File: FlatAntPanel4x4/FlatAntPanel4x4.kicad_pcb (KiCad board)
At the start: 4 copper layers, 186 x 226 mm, 124 parts

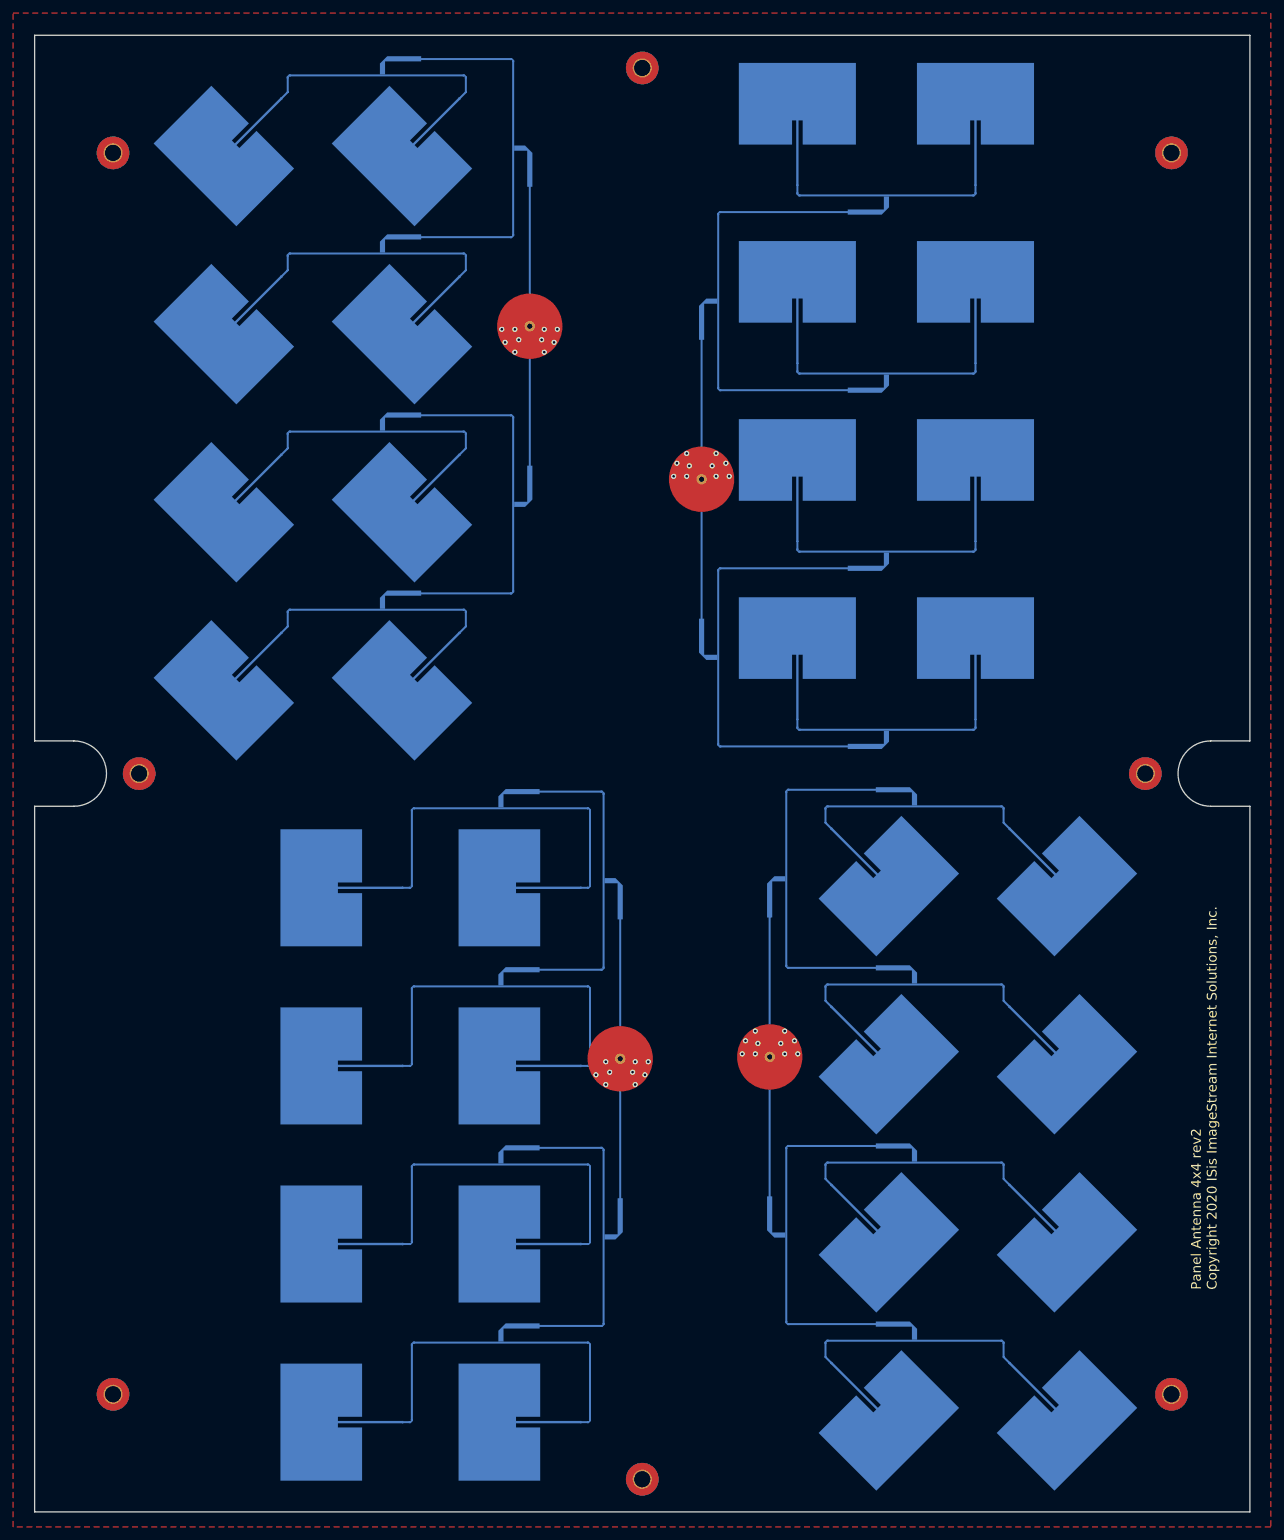
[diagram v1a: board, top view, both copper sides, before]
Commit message: Restore old 4x4 flat antenna. Modify 4 polarity to be 2 pol.
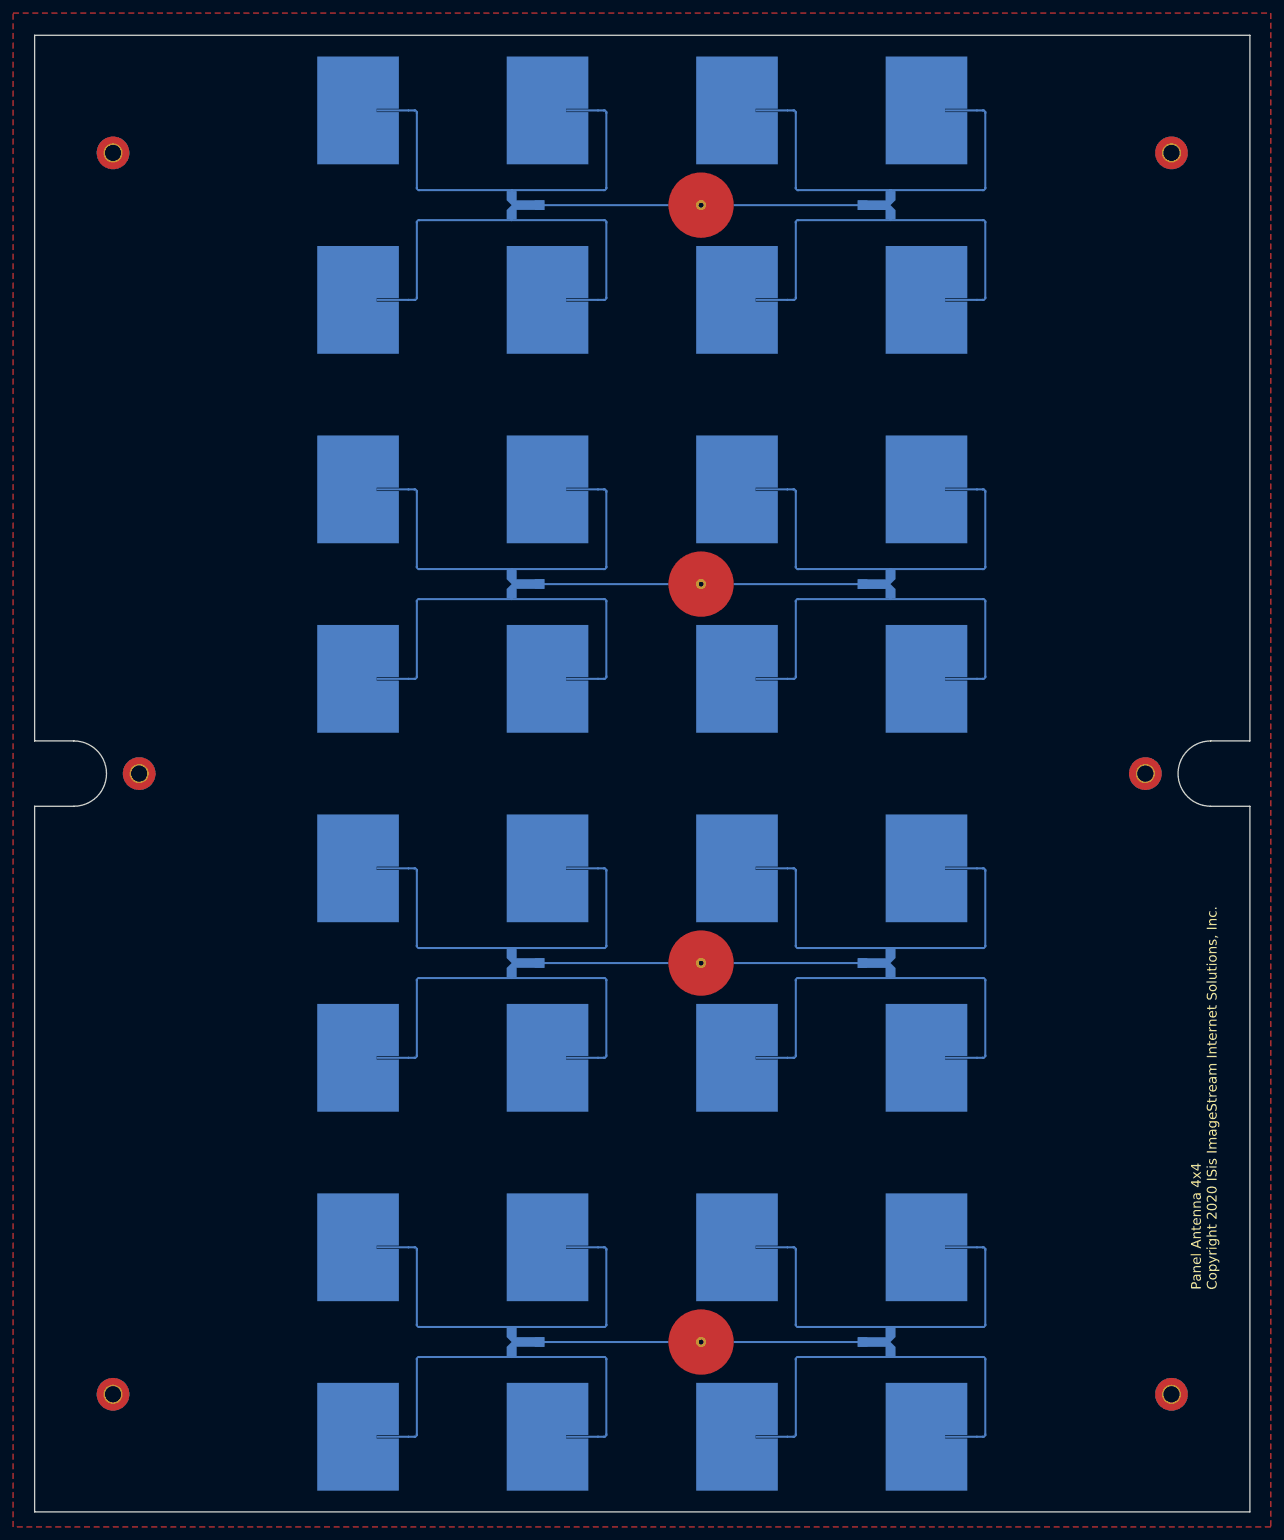
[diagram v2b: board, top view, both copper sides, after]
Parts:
- removed the AA10 at (144.0, 24.5)
- removed the AA10 at (57.7, 118.3)
- removed the AA10 at (144.0, 106.3)
- removed the AA10 at (144.0, 51.8)
- removed the AA10 at (57.7, 172.8)
- removed the AA10 at (57.7, 145.6)
- removed the AA10 at (57.7, 200.1)
- removed the AA10 at (144.0, 79.0)
- removed the AA11 at (85.0, 172.8)
- removed the AA11 at (116.7, 79.0)
- removed the AA11 at (85.0, 200.1)
- removed the AA11 at (116.7, 24.5)
- removed the AA11 at (116.7, 106.3)
- removed the AA11 at (85.0, 118.3)
- removed the AA11 at (116.7, 51.8)
- removed the AA11 at (85.0, 145.6)
- removed the AA12 at (85.0, 185.0)
- removed the AA12 at (85.0, 157.7)
- removed the AA12 at (85.0, 212.3)
- removed the AA12 at (85.0, 130.5)
- removed the AA15 at (104.6, 108.8)
- removed the AA15 at (104.6, 81.6)
- removed the AA15 at (104.6, 54.3)
- removed the AA15 at (87.1, 197.5)
- removed the AA15 at (87.1, 143.0)
- removed the AA15 at (104.6, 27.1)
- removed the AA15 at (87.1, 115.8)
- removed the AA15 at (87.1, 170.3)
- removed the AA5 at (121.0, 199.8)
- removed the AA5 at (148.3, 118.0)
- removed the AA5 at (73.2, 85.4)
- removed the AA5 at (121.0, 145.3)
- removed the AA5 at (148.3, 172.5)
- removed the AA5 at (121.0, 172.5)
- removed the AA5 at (73.2, 30.9)
- removed the AA5 at (73.2, 58.2)
- removed the AA5 at (115.0, 115.5)
- removed the AA5 at (73.2, 3.64)
- removed the AA5 at (38.7, 60.7)
- removed the AA5 at (121.0, 118.0)
- removed the AA5 at (38.7, 87.9)
- removed the AA5 at (115.0, 197.3)
- removed the AA5 at (38.7, 6.14)
- removed the AA5 at (115.0, 142.7)
- removed the AA5 at (66.0, 33.4)
- removed the AA5 at (66.0, 87.9)
- removed the AA5 at (148.3, 145.3)
- removed the AA5 at (38.7, 33.4)
- removed the AA5 at (66.0, 6.14)
- removed the AA5 at (115.0, 170.0)
- removed the AA5 at (148.3, 199.8)
- removed the AA5 at (66.0, 60.7)
- removed the AA9 at (57.7, 212.3)
- removed the AA9 at (57.7, 157.7)
- removed the AA9 at (57.7, 185.0)
- removed the AA9 at (57.7, 130.5)
- removed the AE1 at (43.9, 157.7)
- removed the AE1 at (56.2, 100.3)
- removed the AE1 at (158.0, 157.5)
- removed the AE2 at (29.0, 18.5)
- removed the AE2 at (71.1, 157.7)
- removed the AE2 at (158.0, 130.2)
- removed the AE3 at (29.0, 73.0)
- removed the AE3 at (43.9, 130.5)
- removed the AE3 at (130.7, 157.5)
- removed the AE4 at (71.1, 130.5)
- removed the AE4 at (130.7, 130.2)
- removed the AE4 at (29.0, 45.7)
- removed the AE5 at (43.9, 212.3)
- removed the AE5 at (158.0, 212.0)
- removed the AE5 at (56.2, 45.7)
- removed the AE6 at (56.2, 73.0)
- removed the AE6 at (71.1, 212.3)
- removed the AE6 at (158.0, 184.7)
- removed the AE7 at (56.2, 18.5)
- removed the AE7 at (130.7, 212.0)
- removed the AE7 at (43.9, 185.0)
- removed the AE8 at (130.7, 184.7)
- removed the AE8 at (71.1, 185.0)
- removed the AE8 at (29.0, 100.3)
- removed Feed1 (x4): Feed1, Scott:Flat_Ant_Hole
- removed H10, H9: Mounting Hole, MountingHole:MountingHole_2.5mm_Pad_TopBottom
- removed REF** (x16): RF-Transformer-70.71ohm, Scott-RF-JLCPCB-1.2mm7628-4layer:RF-Transformer-70.71ohm
- removed REF** (x8): RF-Transformer-70.71ohm-Right, Scott-RF-JLCPCB-1.2mm7628-4layer:RF-Transformer-70.71ohm-Right
- added AA1: RFAngle, Scott:RF-Angle-100ohm, B.Cu at (116.5, 98.5)
- added AA1: RFAngle, Scott:RF-Angle-100ohm, B.Cu at (116.5, 40.5)
- added AA1: RFAngle, Scott:RF-Angle-100ohm, B.Cu at (116.5, 156.5)
- added AA1: RFAngle, Scott:RF-Angle-100ohm, B.Cu at (116.5, 214.5)
- added AA10: RFAngle, Scott:RF-Angle-100ohm, B.Cu at (58.5, 86.3)
- added AA10: RFAngle, Scott:RF-Angle-100ohm, B.Cu at (58.5, 202.3)
- added AA10: RFAngle, Scott:RF-Angle-100ohm, B.Cu at (58.5, 144.3)
- added AA10: RFAngle, Scott:RF-Angle-100ohm, B.Cu at (58.5, 28.3)
- added AA11: RFAngle, Scott:RF-Angle-100ohm, B.Cu at (87.5, 144.3)
- added AA11: RFAngle, Scott:RF-Angle-100ohm, B.Cu at (87.5, 202.3)
- added AA11: RFAngle, Scott:RF-Angle-100ohm, B.Cu at (87.5, 28.3)
- added AA11: RFAngle, Scott:RF-Angle-100ohm, B.Cu at (87.5, 86.3)
- added AA12: RFAngle, Scott:RF-Angle-100ohm, B.Cu at (87.5, 156.5)
- added AA12: RFAngle, Scott:RF-Angle-100ohm, B.Cu at (87.5, 98.5)
- added AA12: RFAngle, Scott:RF-Angle-100ohm, B.Cu at (87.5, 214.5)
- added AA12: RFAngle, Scott:RF-Angle-100ohm, B.Cu at (87.5, 40.5)
- added AA13: RFAngle, Scott:RF-Angle-100ohm, B.Cu at (58.5, 127.5)
- added AA13: RFAngle, Scott:RF-Angle-100ohm, B.Cu at (58.5, 185.5)
- added AA13: RFAngle, Scott:RF-Angle-100ohm, B.Cu at (58.5, 69.5)
- added AA13: RFAngle, Scott:RF-Angle-100ohm, B.Cu at (58.5, 11.5)
- added AA14: RFAngle, Scott:RF-Angle-100ohm, B.Cu at (58.5, 139.7)
- added AA14: RFAngle, Scott:RF-Angle-100ohm, B.Cu at (58.5, 197.7)
- added AA14: RFAngle, Scott:RF-Angle-100ohm, B.Cu at (58.5, 81.7)
- added AA14: RFAngle, Scott:RF-Angle-100ohm, B.Cu at (58.5, 23.7)
- added AA15: RFAngle, Scott:RF-Angle-100ohm, B.Cu at (87.5, 81.7)
- added AA15: RFAngle, Scott:RF-Angle-100ohm, B.Cu at (87.5, 197.7)
- added AA15: RFAngle, Scott:RF-Angle-100ohm, B.Cu at (87.5, 139.7)
- added AA15: RFAngle, Scott:RF-Angle-100ohm, B.Cu at (87.5, 23.7)
- added AA16: RFAngle, Scott:RF-Angle-100ohm, B.Cu at (87.5, 69.5)
- added AA16: RFAngle, Scott:RF-Angle-100ohm, B.Cu at (87.5, 11.5)
- added AA16: RFAngle, Scott:RF-Angle-100ohm, B.Cu at (87.5, 127.5)
- added AA16: RFAngle, Scott:RF-Angle-100ohm, B.Cu at (87.5, 185.5)
- added AA2: RFAngle, Scott:RF-Angle-100ohm, B.Cu at (116.5, 28.3)
- added AA2: RFAngle, Scott:RF-Angle-100ohm, B.Cu at (116.5, 202.3)
- added AA2: RFAngle, Scott:RF-Angle-100ohm, B.Cu at (116.5, 144.3)
- added AA2: RFAngle, Scott:RF-Angle-100ohm, B.Cu at (116.5, 86.3)
- added AA3: RFAngle, Scott:RF-Angle-100ohm, B.Cu at (145.5, 144.3)
- added AA3: RFAngle, Scott:RF-Angle-100ohm, B.Cu at (145.5, 202.3)
- added AA3: RFAngle, Scott:RF-Angle-100ohm, B.Cu at (145.5, 86.3)
- added AA3: RFAngle, Scott:RF-Angle-100ohm, B.Cu at (145.5, 28.3)
- added AA4: RFAngle, Scott:RF-Angle-100ohm, B.Cu at (145.5, 40.5)
- added AA4: RFAngle, Scott:RF-Angle-100ohm, B.Cu at (145.5, 214.5)
- added AA4: RFAngle, Scott:RF-Angle-100ohm, B.Cu at (145.5, 98.5)
- added AA4: RFAngle, Scott:RF-Angle-100ohm, B.Cu at (145.5, 156.5)
- added AA5: RFAngle, Scott:RF-Angle-100ohm, B.Cu at (116.5, 185.5)
- added AA5: RFAngle, Scott:RF-Angle-100ohm, B.Cu at (116.5, 127.5)
- added AA5: RFAngle, Scott:RF-Angle-100ohm, B.Cu at (116.5, 69.5)
- added AA5: RFAngle, Scott:RF-Angle-100ohm, B.Cu at (116.5, 11.5)
- added AA6: RFAngle, Scott:RF-Angle-100ohm, B.Cu at (116.5, 23.7)
- added AA6: RFAngle, Scott:RF-Angle-100ohm, B.Cu at (116.5, 197.7)
- added AA6: RFAngle, Scott:RF-Angle-100ohm, B.Cu at (116.5, 139.7)
- added AA6: RFAngle, Scott:RF-Angle-100ohm, B.Cu at (116.5, 81.7)
- added AA7: RFAngle, Scott:RF-Angle-100ohm, B.Cu at (145.5, 81.7)
- added AA7: RFAngle, Scott:RF-Angle-100ohm, B.Cu at (145.5, 197.7)
- added AA7: RFAngle, Scott:RF-Angle-100ohm, B.Cu at (145.5, 23.7)
- added AA7: RFAngle, Scott:RF-Angle-100ohm, B.Cu at (145.5, 139.7)
- added AA8: RFAngle, Scott:RF-Angle-100ohm, B.Cu at (145.5, 127.5)
- added AA8: RFAngle, Scott:RF-Angle-100ohm, B.Cu at (145.5, 11.5)
- added AA8: RFAngle, Scott:RF-Angle-100ohm, B.Cu at (145.5, 69.5)
- added AA8: RFAngle, Scott:RF-Angle-100ohm, B.Cu at (145.5, 185.5)
- added AA9: RFAngle, Scott:RF-Angle-100ohm, B.Cu at (58.5, 156.5)
- added AA9: RFAngle, Scott:RF-Angle-100ohm, B.Cu at (58.5, 40.5)
- added AA9: RFAngle, Scott:RF-Angle-100ohm, B.Cu at (58.5, 214.5)
- added AA9: RFAngle, Scott:RF-Angle-100ohm, B.Cu at (58.5, 98.5)
- added AE1: Antenna, Scott:PanelAnt5.0_V_UP_100R, B.Cu at (107.5, 40.5)
- added AE1: Antenna, Scott:PanelAnt5.0_V_UP_100R, B.Cu at (107.5, 156.5)
- added AE1: Antenna, Scott:PanelAnt5.0_V_UP_100R, B.Cu at (107.5, 98.5)
- added AE2: Antenna, Scott:PanelAnt5.0_V_UP_100R, B.Cu at (136.5, 156.5)
- added AE2: Antenna, Scott:PanelAnt5.0_V_UP_100R, B.Cu at (136.5, 40.5)
- added AE2: Antenna, Scott:PanelAnt5.0_V_UP_100R, B.Cu at (136.5, 98.5)
- added AE3: Antenna, Scott:PanelAnt5.0_V_UP_100R, B.Cu at (107.5, 11.5)
- added AE3: Antenna, Scott:PanelAnt5.0_V_UP_100R, B.Cu at (107.5, 69.5)
- added AE3: Antenna, Scott:PanelAnt5.0_V_UP_100R, B.Cu at (107.5, 127.5)
- added AE4: Antenna, Scott:PanelAnt5.0_V_UP_100R, B.Cu at (136.5, 127.5)
- added AE4: Antenna, Scott:PanelAnt5.0_V_UP_100R, B.Cu at (136.5, 11.5)
- added AE4: Antenna, Scott:PanelAnt5.0_V_UP_100R, B.Cu at (136.5, 69.5)
- added AE5: Antenna, Scott:PanelAnt5.0_V_UP_100R, B.Cu at (49.5, 98.5)
- added AE5: Antenna, Scott:PanelAnt5.0_V_UP_100R, B.Cu at (49.5, 40.5)
- added AE5: Antenna, Scott:PanelAnt5.0_V_UP_100R, B.Cu at (49.5, 156.5)
- added AE6: Antenna, Scott:PanelAnt5.0_V_UP_100R, B.Cu at (78.5, 98.5)
- added AE6: Antenna, Scott:PanelAnt5.0_V_UP_100R, B.Cu at (78.5, 40.5)
- added AE6: Antenna, Scott:PanelAnt5.0_V_UP_100R, B.Cu at (78.5, 156.5)
- added AE7: Antenna, Scott:PanelAnt5.0_V_UP_100R, B.Cu at (49.5, 127.5)
- added AE7: Antenna, Scott:PanelAnt5.0_V_UP_100R, B.Cu at (49.5, 69.5)
- added AE7: Antenna, Scott:PanelAnt5.0_V_UP_100R, B.Cu at (49.5, 11.5)
- added AE8: Antenna, Scott:PanelAnt5.0_V_UP_100R, B.Cu at (78.5, 127.5)
- added AE8: Antenna, Scott:PanelAnt5.0_V_UP_100R, B.Cu at (78.5, 11.5)
- added AE8: Antenna, Scott:PanelAnt5.0_V_UP_100R, B.Cu at (78.5, 69.5)
- added FEED 1: Feed1, Scott:Flat_Ant_Hole, B.Cu at (102.0, 26.0)
- added FEED 2: Feed1, Scott:Flat_Ant_Hole, B.Cu at (102.0, 84.0)
- added FEED 3: Feed1, Scott:Flat_Ant_Hole, B.Cu at (102.0, 142.0)
- added FEED 4: Feed1, Scott:Flat_Ant_Hole, B.Cu at (102.0, 200.0)
- added NT1: NetTie_3_Tee, Scott:RF-T-50ohm, B.Cu at (131.0, 84.0)
- added NT1: NetTie_3_Tee, Scott:RF-T-50ohm, B.Cu at (131.0, 142.0)
- added NT1: NetTie_3_Tee, Scott:RF-T-50ohm, B.Cu at (131.0, 26.0)
- added NT1: NetTie_3_Tee, Scott:RF-T-50ohm, B.Cu at (131.0, 200.0)
- added NT2: NetTie_3_Tee, Scott:RF-T-50ohm, B.Cu at (73.0, 200.0)
- added NT2: NetTie_3_Tee, Scott:RF-T-50ohm, B.Cu at (73.0, 26.0)
- added NT2: NetTie_3_Tee, Scott:RF-T-50ohm, B.Cu at (73.0, 142.0)
- added NT2: NetTie_3_Tee, Scott:RF-T-50ohm, B.Cu at (73.0, 84.0)
- AE1, AE2, AE3, AE4, AE5, AE6, AE7, AE8: footprint Scott-RF-JLCPCB-1.2mm7628-4layer:Patch_Inset_5.5_Linear_7.1dBi_100R -> Scott:PanelAnt5.0_V_UP_100R
- moved AE5 214.8 mm to (49.5, 214.5), turned to 90 degrees
- moved AE7 198.9 mm to (49.5, 185.5), turned to 90 degrees
- moved AE6 180.8 mm to (78.5, 214.5), turned to 90 degrees
- moved AE8 161.6 mm to (78.5, 185.5), turned to 90 degrees
- moved AE1 149.8 mm to (107.5, 214.5), turned to 90 degrees
- moved AE3 125.9 mm to (107.5, 185.5), turned to 90 degrees
- moved AE2 123.8 mm to (136.5, 214.5), turned to 90 degrees
- moved AE4 93.5 mm to (136.5, 185.5), turned to 90 degrees
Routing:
- net /A1E3S2: track 293.9 -> 46.4 mm
- net /A1P1: track 397.6 -> 196.0 mm
- net /A1E3: track 194.7 -> 3.81 mm
- net /A1P3: track 0.00 -> 116.9 mm
- net /A1P2: track 0.00 -> 116.9 mm
- net /A1P5: track 0.00 -> 116.4 mm
- net /A1P4: track 212.9 -> 117.1 mm
- net /A1E4S2: track 0.00 -> 46.4 mm
- net /A1E8S2: track 0.00 -> 46.3 mm
- net /A1E7S2: track 0.00 -> 46.3 mm
- net /A1E1S2: track 0.00 -> 45.6 mm
- net /A1E2S2: track 0.00 -> 45.6 mm
- net /A1E6S2: track 51.2 -> 45.6 mm
- net /A1E5S2: track 51.3 -> 46.0 mm
- net /A1E8: track 0.00 -> 3.88 mm
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- added copper zone on F.Cu, net GND
- removed copper zone on F.Cu, net (none)
- removed copper zone on In1.Cu, net GND
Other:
- copper layers 4 -> 2
- board text added: "Panel Antenna 4x4 Copyright 2020 ISis ImageStream Internet Solutions, Inc."
- board text removed: "Panel Antenna 4x4 rev2 Copyright 2020 ISis ImageStream Internet Solutions, Inc."

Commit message: Many enhancements to the AP3000 board. Reworking FlatAntPanel4x4 again with proper holes Made a connector test pcb
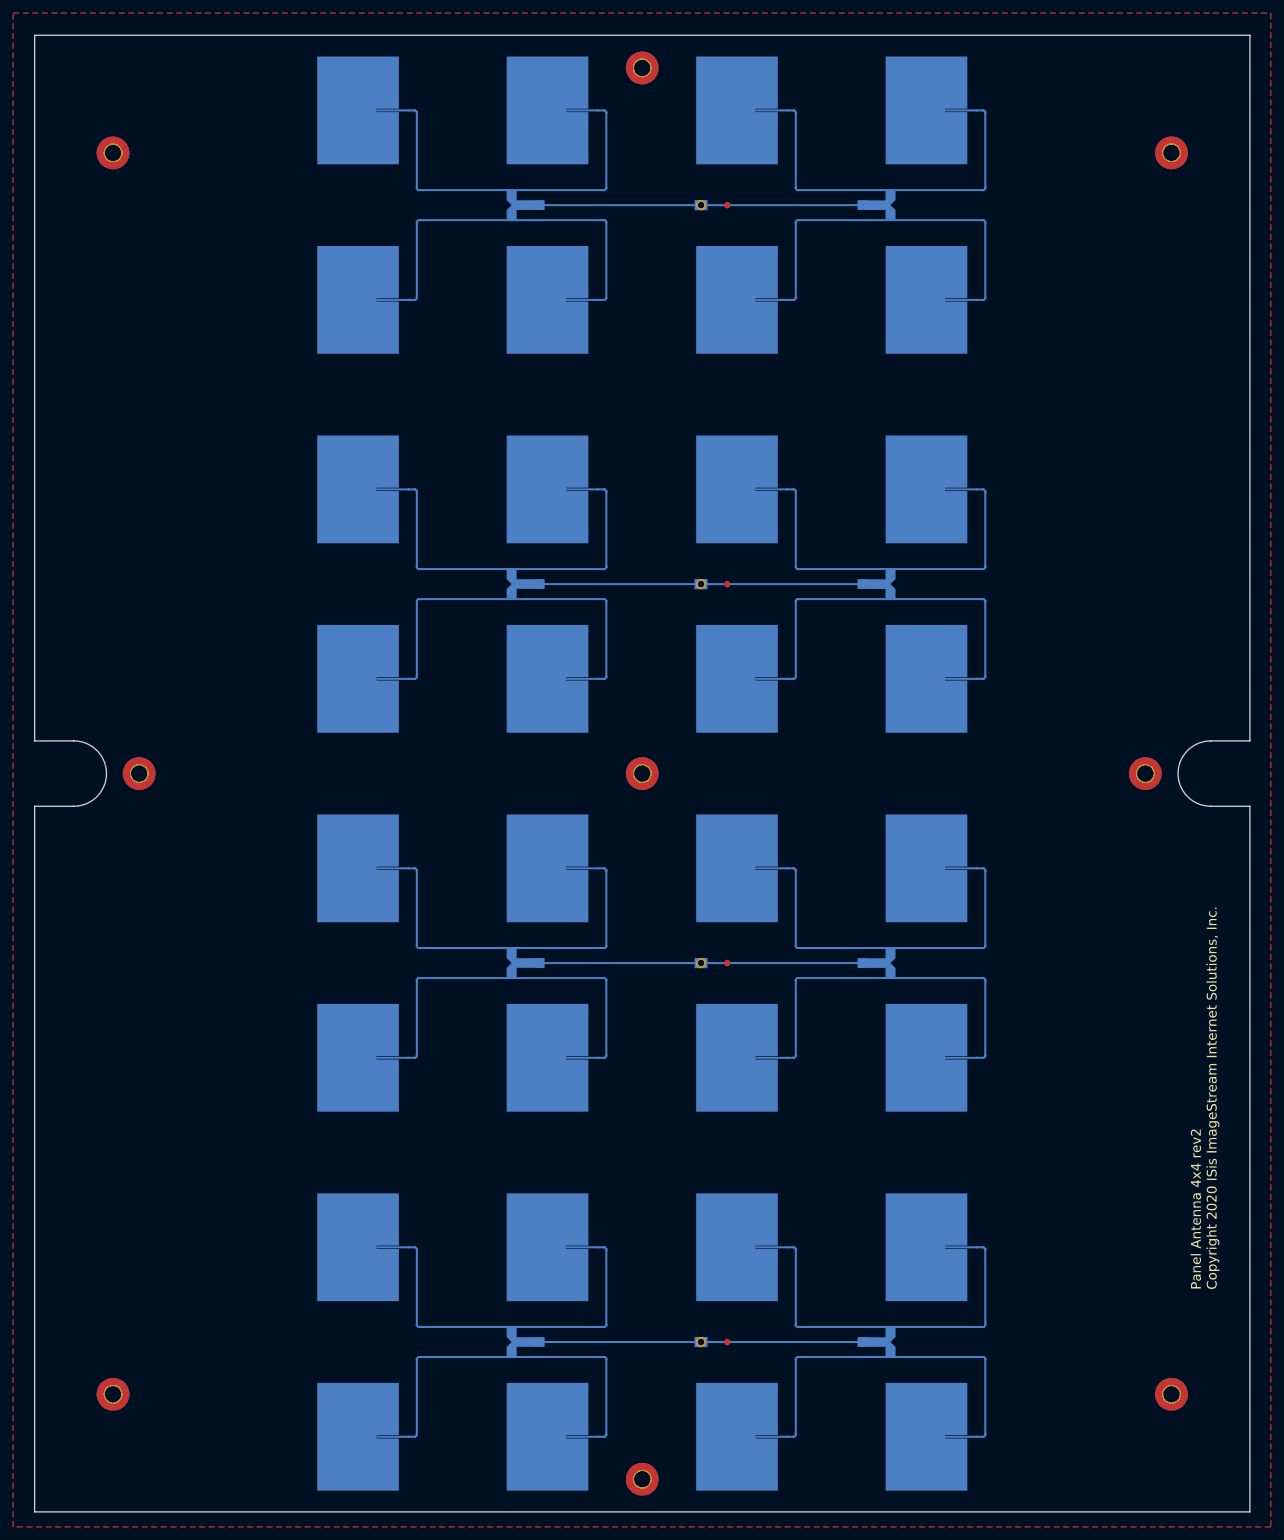
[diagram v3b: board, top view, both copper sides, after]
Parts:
- added H10: Mounting Hole, MountingHole:MountingHole_2.5mm_Pad_TopBottom, F.Cu at (93.0, 5.00)
- added H12: Mounting Hole, MountingHole:MountingHole_2.5mm_Pad_TopBottom, F.Cu at (93.0, 113.0)
- added H9: Mounting Hole, MountingHole:MountingHole_2.5mm_Pad_TopBottom, F.Cu at (93.0, 221.0)
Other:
- board text added: "Panel Antenna 4x4 rev2 Copyright 2020 ISis ImageStream Internet Solutions, Inc."
- board text removed: "Panel Antenna 4x4 Copyright 2020 ISis ImageStream Internet Solutions, Inc."
